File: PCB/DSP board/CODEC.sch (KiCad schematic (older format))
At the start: 23 parts, among them U3 CS42448

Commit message: Schematics + Footprints Rev.1
Ready to route.
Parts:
- C62, C65, C68, C69, C70, C72, C73, C74, C75, C76, C77, C78, C79, C80: footprint (none) -> Capacitors_SMD:C_0603
- C63: footprint (none) -> Capacitors_Tantalum_SMD:CP_Tantalum_Case-A_EIA-3216-18_Reflow
- C64, C67, C71: footprint (none) -> Capacitors_SMD:C_0805
- C66: footprint (none) -> Capacitors_Tantalum_SMD:CP_Tantalum_Case-B_EIA-3528-21_Reflow
- L4: footprint (none) -> Inductors_SMD:L_0603
- RN11, RN12: footprint (none) -> Resistor:0603_RN4
- U3: footprint (none) -> Housings_QFP:LQFP-64_10x10mm_Pitch0.5mm

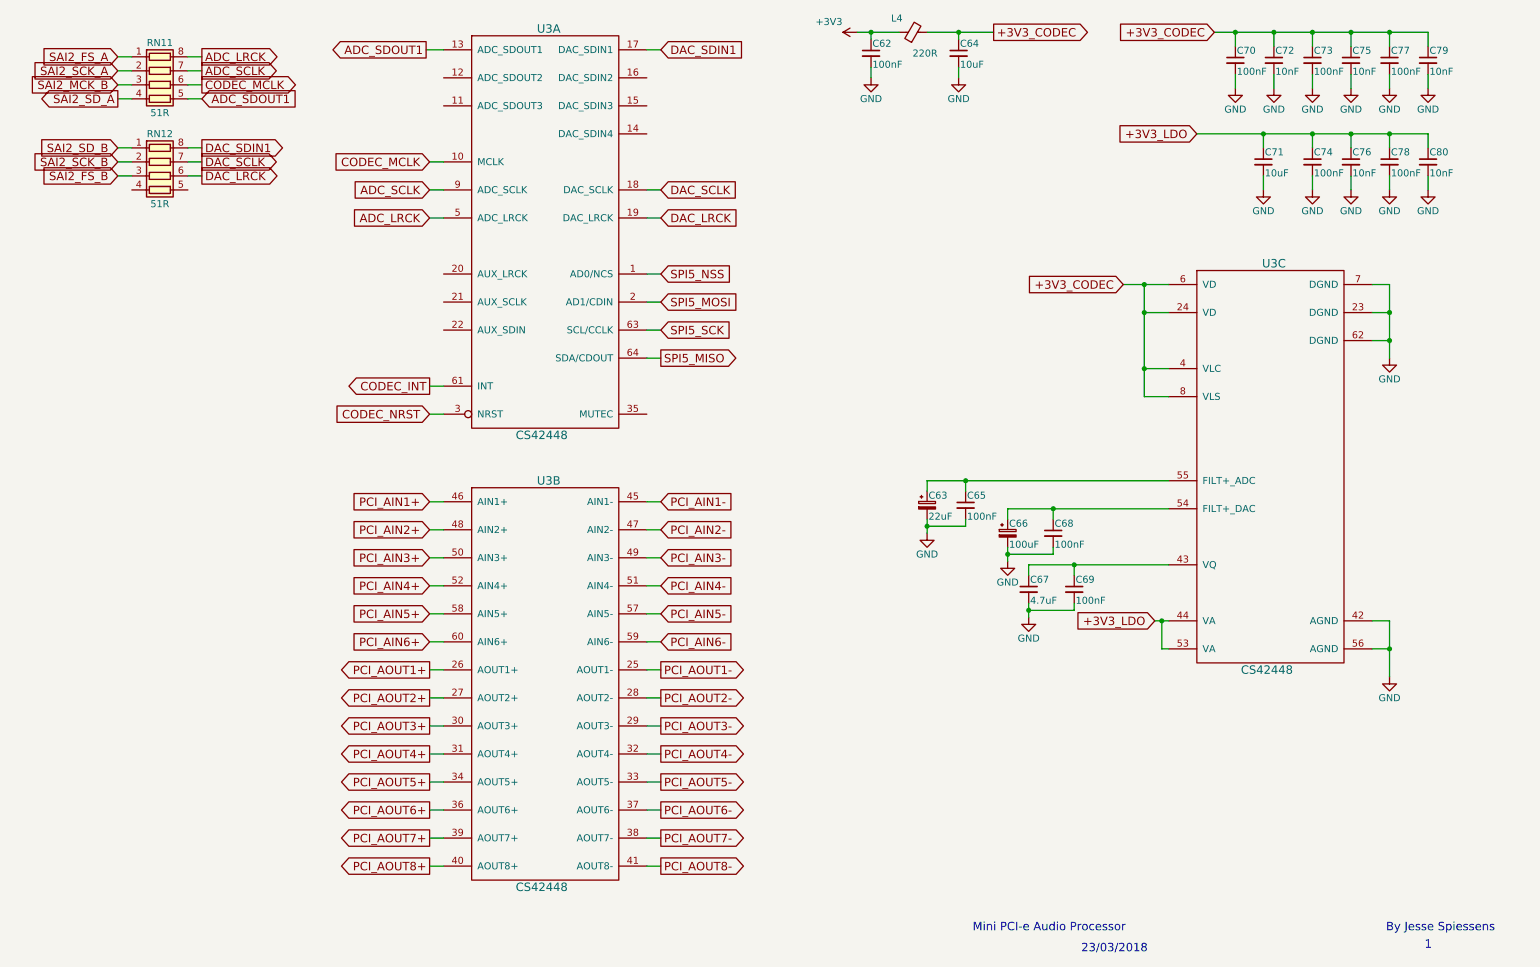
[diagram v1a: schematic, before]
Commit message: Schematics & PCB
Schematics update - ERC error fixing
PCB - setup & PCB outline
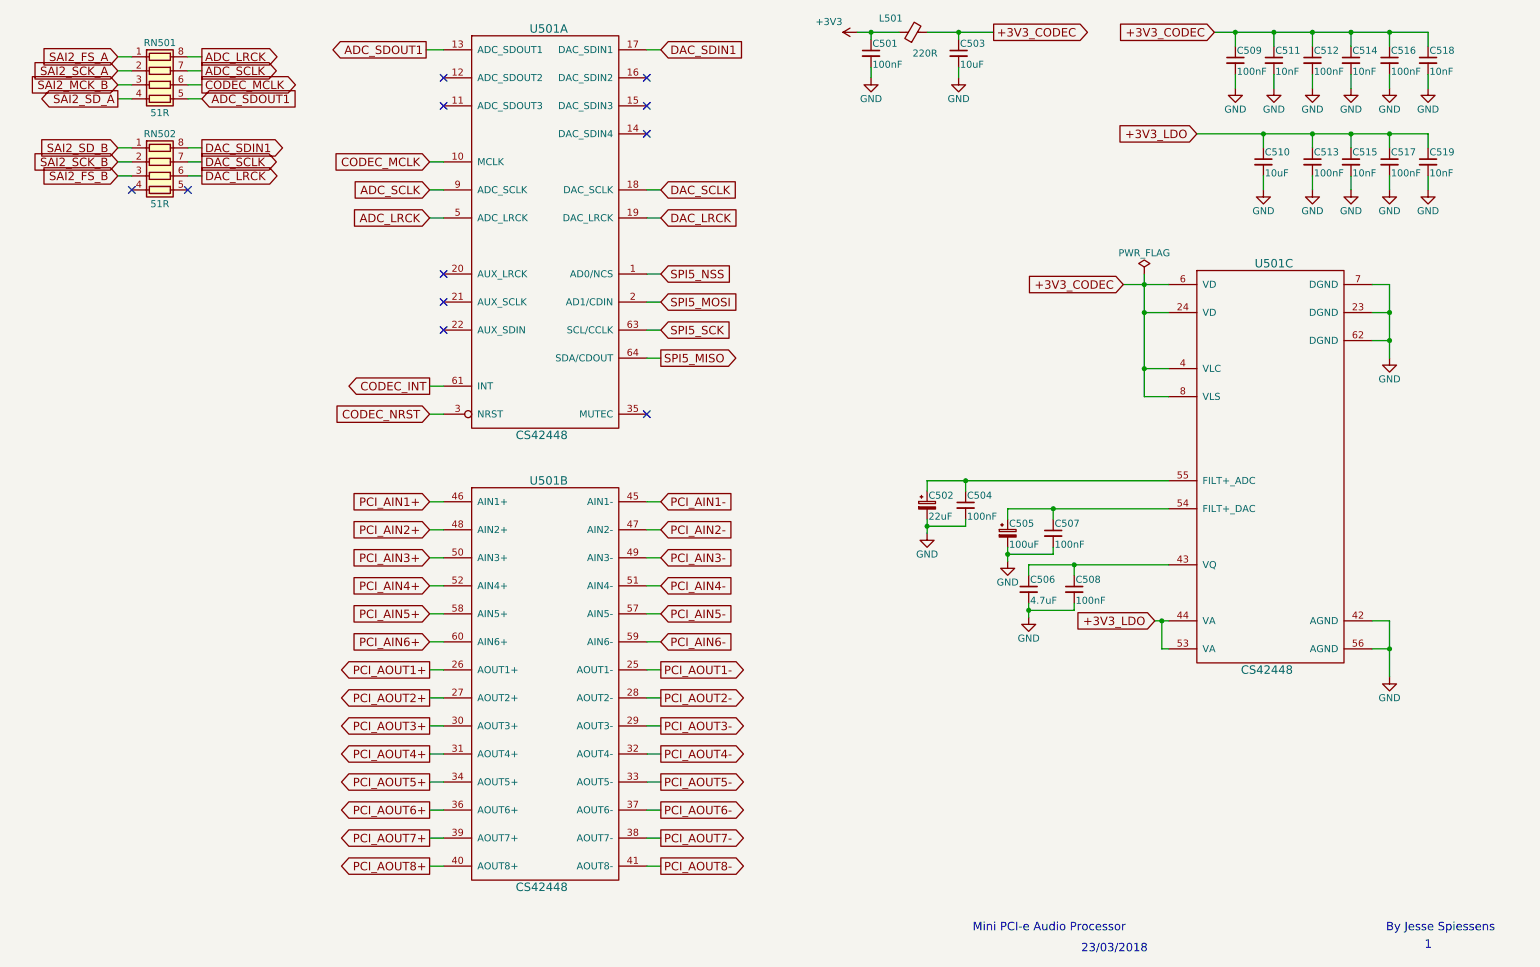
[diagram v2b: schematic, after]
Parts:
- renumbered C62 to C501, C63 to C502, C64 to C503, C65 to C504, C66 to C505, C67 to C506, C68 to C507, C69 to C508, C70 to C509, C71 to C510, C72 to C511, C73 to C512, C74 to C513, C75 to C514, C76 to C515, C77 to C516, C78 to C517, C79 to C518, C80 to C519, L4 to L501, RN11 to RN501, RN12 to RN502, U3 to U501
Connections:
- no-connect marks 0 -> 11

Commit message: Schematic updates + PCB placement
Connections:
- net DAC_LRCK: now also RN502.5 (R4.2); no longer RN502.6 (R3.2)
- net DAC_SCLK: now also RN502.6 (R3.2); no longer RN502.7 (R2.2)
- net DAC_SDIN1: now also RN502.7 (R2.2); no longer RN502.8 (R1.2)
- net SAI2_FS_B: now also RN502.4 (R4.1); no longer RN502.3 (R3.1)
- net SAI2_SCK_B: now also RN502.3 (R3.1); no longer RN502.2 (R2.1)
- net SAI2_SD_B: now also RN502.2 (R2.1); no longer RN502.1 (R1.1)
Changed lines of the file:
@@
 Text GLabel 1225 1550 0    60   Output ~ 0
 SAI2_SD_A
-Text GLabel 1225 1900 0    60   Input ~ 0
+Text GLabel 1225 2000 0    60   Input ~ 0
 SAI2_SD_B
-Text GLabel 1225 2000 0    60   Input ~ 0
+Text GLabel 1225 2100 0    60   Input ~ 0
 SAI2_SCK_B
-Text GLabel 1225 2100 0    60   Input ~ 0
+Text GLabel 1225 2200 0    60   Input ~ 0
 SAI2_FS_B
 Text GLabel 1825 1250 2    60   Output ~ 0
@@
 Text GLabel 1825 1550 2    60   Input ~ 0
 ADC_SDOUT1
-Text GLabel 1825 1900 2    60   Output ~ 0
+Text GLabel 1825 2000 2    60   Output ~ 0
 DAC_SDIN1
-Text GLabel 1825 2000 2    60   Output ~ 0
+Text GLabel 1825 2100 2    60   Output ~ 0
 DAC_SCLK
-Text GLabel 1825 2100 2    60   Output ~ 0
+Text GLabel 1825 2200 2    60   Output ~ 0
 DAC_LRCK
 Text GLabel 3450 2400 0    60   Input ~ 0
@@
 	1325 1550 1225 1550
 Wire Wire Line
-	1225 1900 1325 1900
-Wire Wire Line
-	1325 2000 1225 2000
-Wire Wire Line
-	1225 2100 1325 2100
+	1225 2000 1325 2000
+Wire Wire Line
+	1325 2100 1225 2100
+Wire Wire Line
+	1225 2200 1325 2200
 Wire Wire Line
 	1725 1250 1825 1250
@@
 	3450 2400 3550 2400
 Wire Wire Line
-	1725 1900 1825 1900
-Wire Wire Line
-	1825 2000 1725 2000
-Wire Wire Line
-	1725 2100 1825 2100
+	1725 2000 1825 2000
+Wire Wire Line
+	1825 2100 1725 2100
+Wire Wire Line
+	1725 2200 1825 2200
 Wire Wire Line
 	5000 1200 5100 1200
@@
 NoConn ~ 5000 1800
 NoConn ~ 5000 3800
-NoConn ~ 1725 2200
-NoConn ~ 1325 2200
 NoConn ~ 3550 2800
 NoConn ~ 3550 3000
@@
 	1    0    0    -1
 $EndComp
+NoConn ~ 1325 1900
+NoConn ~ 1725 1900
 $EndSCHEMATC
